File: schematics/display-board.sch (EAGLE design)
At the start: 245 parts

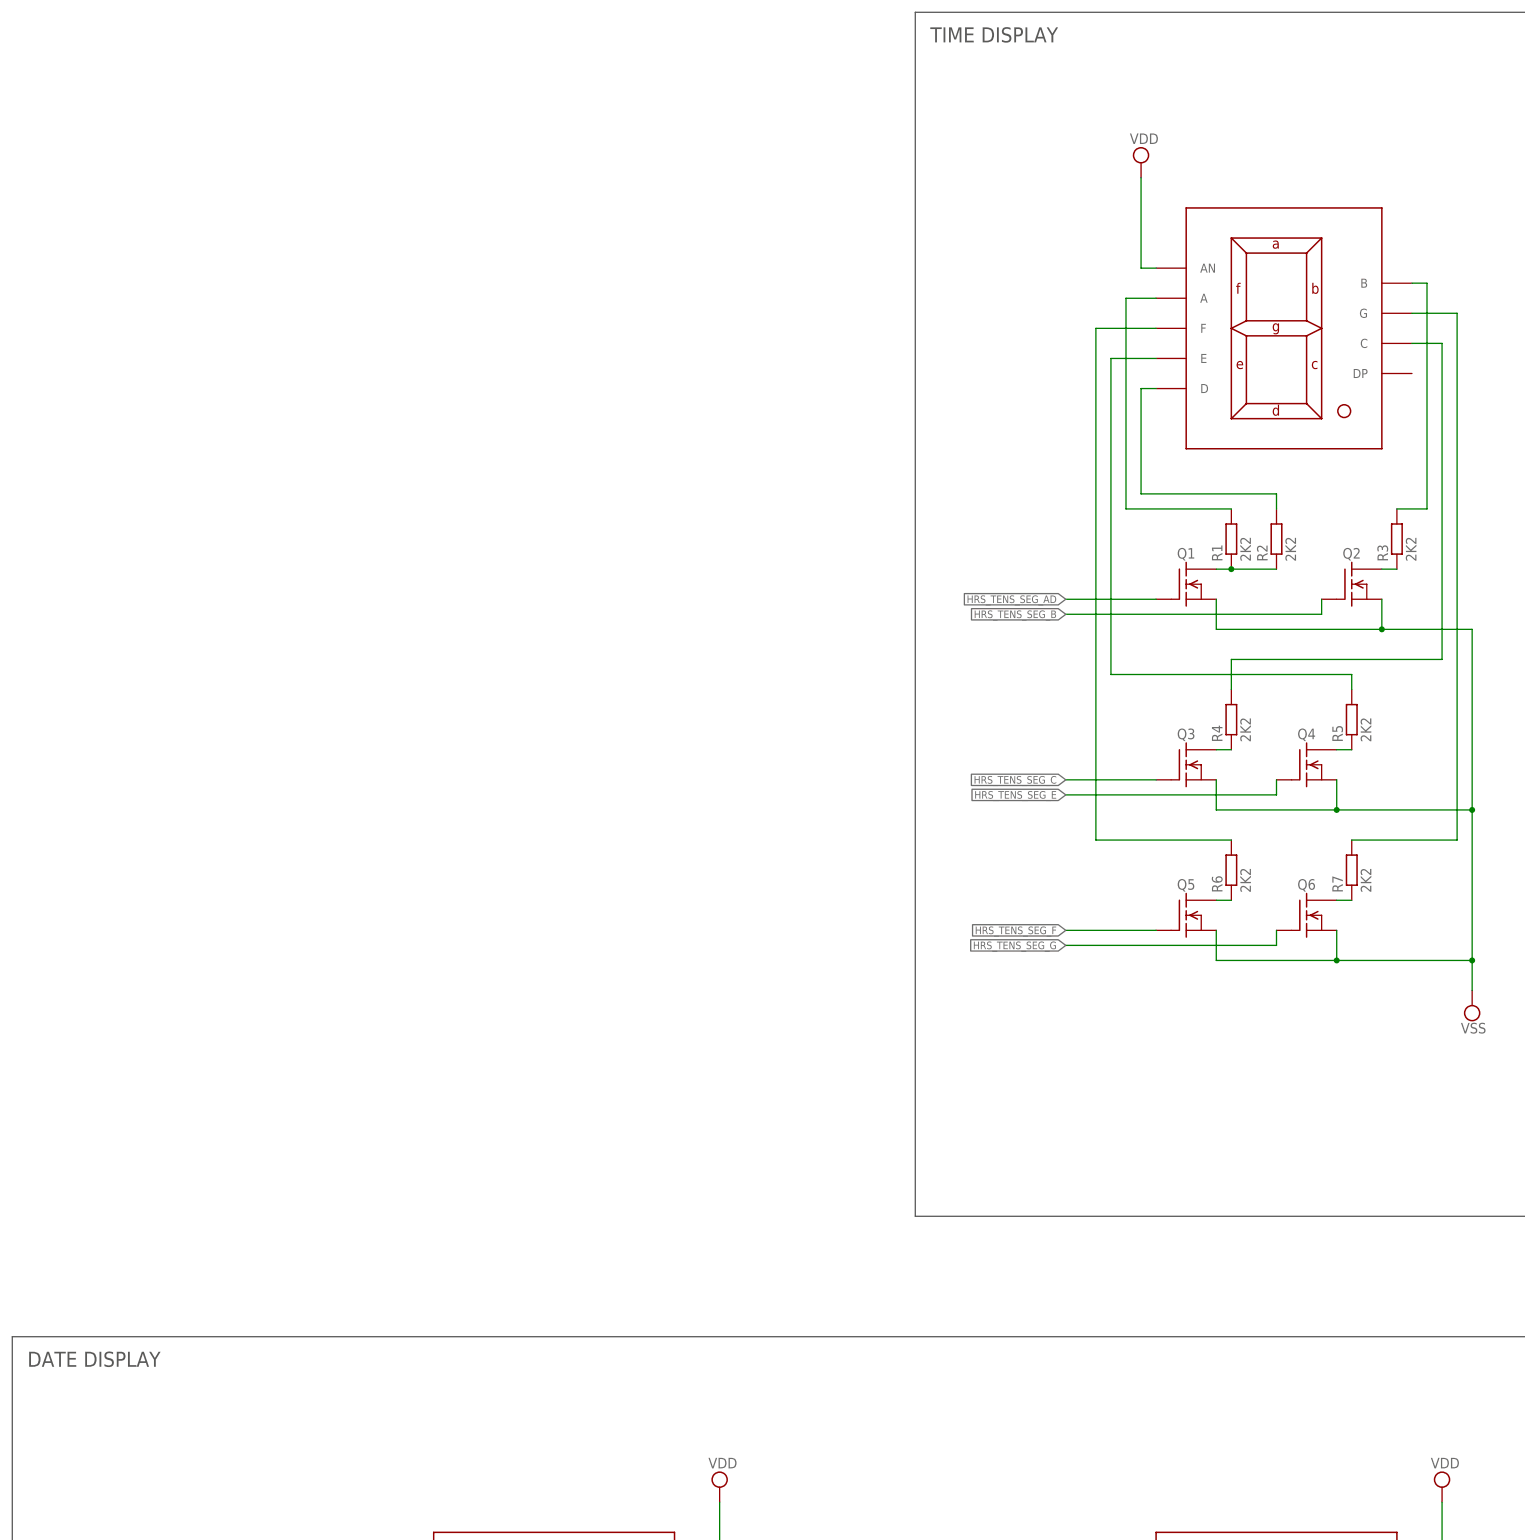
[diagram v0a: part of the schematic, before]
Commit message: Add display part numbers to display board shematics
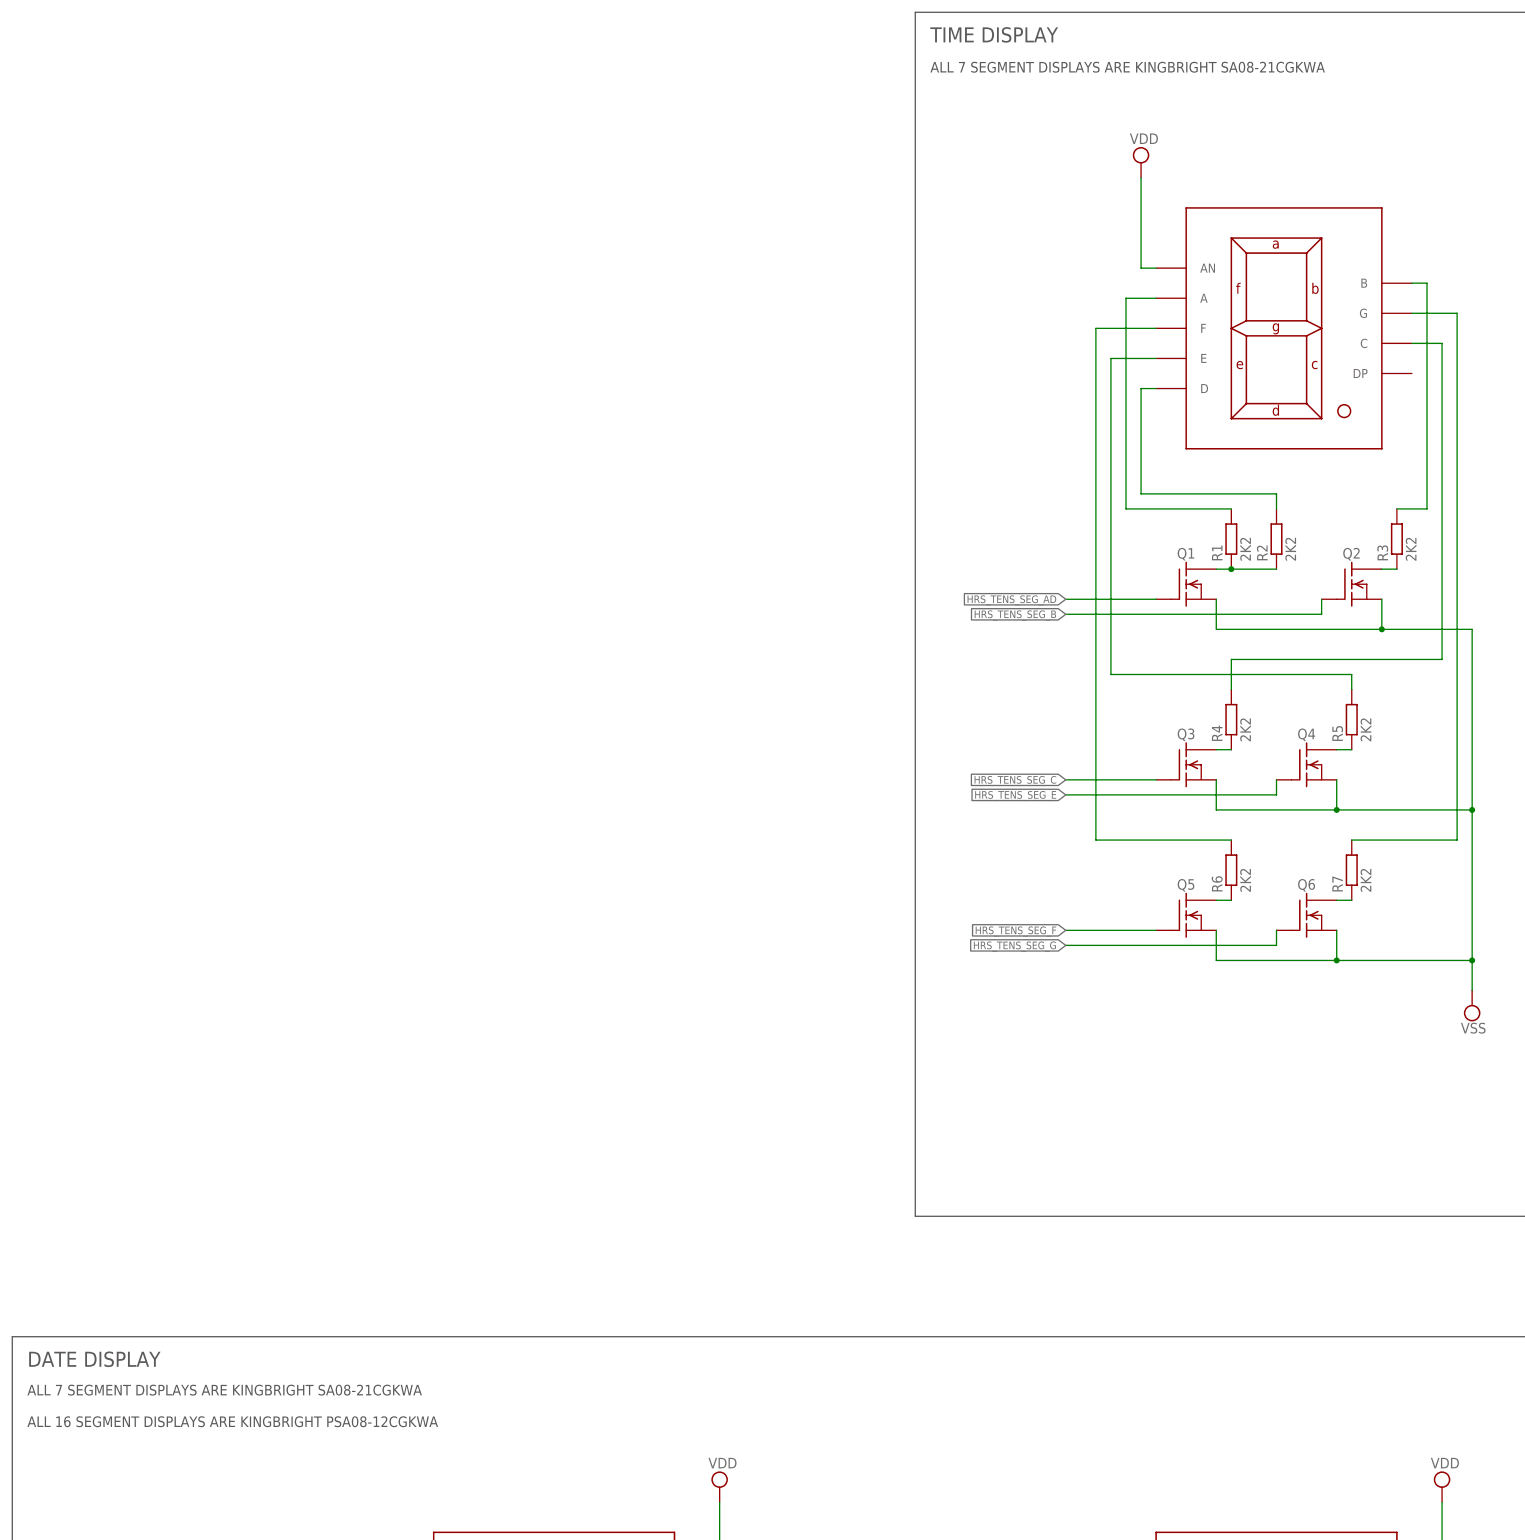
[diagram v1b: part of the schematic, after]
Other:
- note added: "ALL 7 SEGMENT DISPLAYS ARE KINGBRIGHT SA08-21CGKWA"
- note added: "ALL 7 SEGMENT DISPLAYS ARE KINGBRIGHT SA08-21CGKWA ALL 16 SEGMENT DISPLAYS ARE KINGBRIGHT PSA08-12CGKWA"
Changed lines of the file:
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@@
 <wire x1="93.98" y1="271.78" x2="93.98" y2="495.3" width="0.1524" layer="97"/>
 <text x="96.52" y="492.76" size="2.54" layer="97" align="top-left">DATE DISPLAY</text>
+<text x="96.52" y="480.06" size="1.778" layer="97">ALL 7 SEGMENT DISPLAYS ARE KINGBRIGHT SA08-21CGKWA
+ALL 16 SEGMENT DISPLAYS ARE KINGBRIGHT PSA08-12CGKWA</text>
+<text x="248.92" y="708.66" size="1.778" layer="97">ALL 7 SEGMENT DISPLAYS ARE KINGBRIGHT SA08-21CGKWA</text>
 </plain>
 <instances>
@@
 </schematic>
 </drawing>
+<compatibility>
+<note version="6.3" minversion="6.2.2" severity="warning">
+Since Version 6.2.2 text objects can contain more than one line,
+which will not be processed correctly with this version.
+</note>
+</compatibility>
 </eagle>
